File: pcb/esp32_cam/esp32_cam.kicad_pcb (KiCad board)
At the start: 2 copper layers, 31.3 x 43.3 mm, 45 parts, among them CN1 ESP32CAM_P1, CN2 ESP-PSRAM32, CN3 Cam_Connector, CN4 ESP32CAM_P2, CN5 microSD_esp32Cam, Q1 S8050, Q2 PMOS, SW1 SWITCH, U1 ESP32-S(CAM), U2 AMS1117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

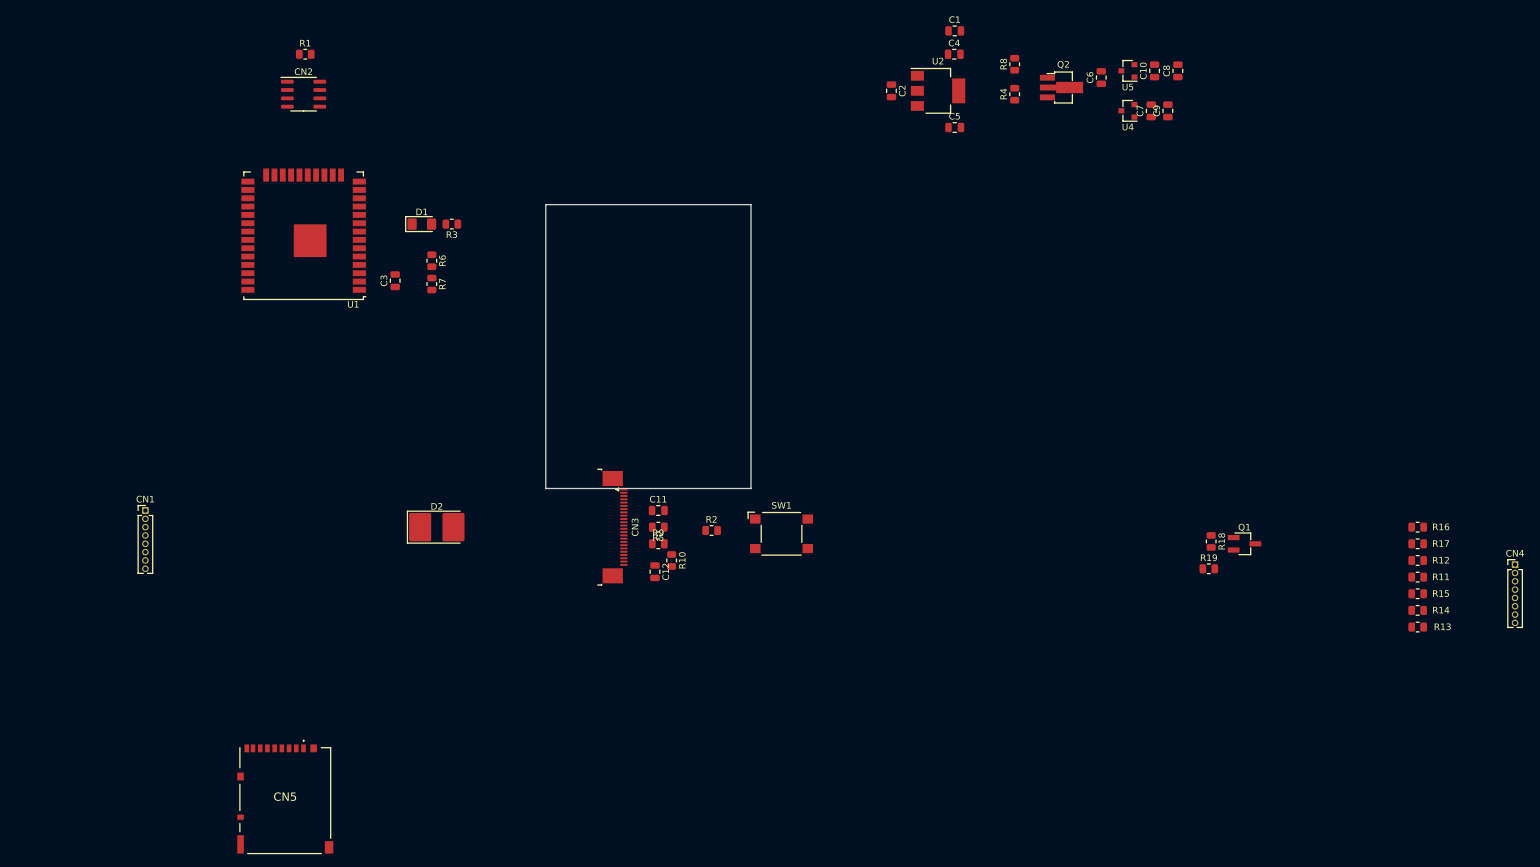
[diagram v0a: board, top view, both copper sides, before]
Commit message: correcciones de esquematico y se agrega y completa  información
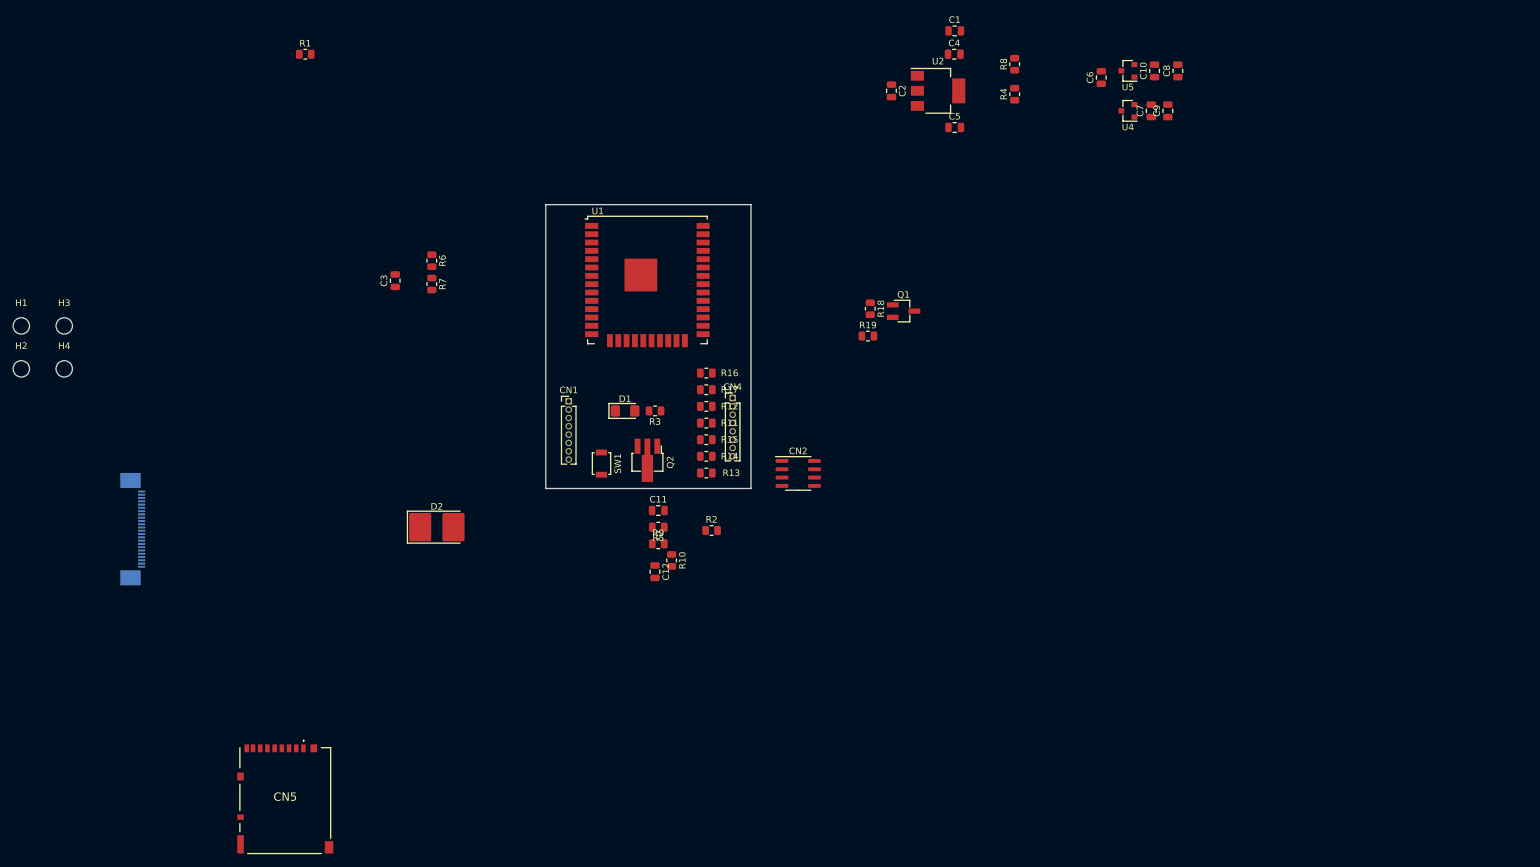
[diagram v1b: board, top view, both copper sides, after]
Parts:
- added H1: MountingHole, MountingHole:MountingHole_2.5mm, F.Cu at (-30.0, 68.5)
- added H2: MountingHole, MountingHole:MountingHole_2.5mm, F.Cu at (-30.0, 75.0)
- added H3: MountingHole, MountingHole:MountingHole_2.5mm, F.Cu at (-23.4, 68.5)
- added H4: MountingHole, MountingHole:MountingHole_2.5mm, F.Cu at (-23.4, 75.0)
- CN3: moved to B.Cu
- SW1: footprint Button_Switch_SMD:SW_SPST_Omron_B3FS-101xP -> Button_Switch_SMD:SW_SPST_B3U-1000P
- moved CN4 122.0 mm to (78.5, 79.5)
- moved R11 111.0 mm to (74.5, 83.3)
- moved R12 111.0 mm to (74.5, 80.8)
- moved R13 111.0 mm to (74.5, 90.9)
- moved R14 111.0 mm to (74.5, 88.4)
- moved R15 111.0 mm to (74.5, 85.9)
- moved R16 111.0 mm to (74.5, 75.7)
- moved R17 111.0 mm to (74.5, 78.2)
- moved CN2 95.1 mm to (88.5, 91.0)
- moved Q2 85.0 mm to (65.5, 89.0), turned to 270 degrees
- moved CN3 73.6 mm to (-13.0, 99.5), turned to 90 degrees
- moved CN1 66.7 mm to (53.5, 80.0)
- moved Q1 63.0 mm to (104.6, 66.2)
- moved R19 63.0 mm to (99.1, 70.0)
- moved R18 63.0 mm to (99.5, 65.9)
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
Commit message: se sube primera versión del PCB
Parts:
- C10, C11, C12, C3, C6, C7, C8, C9, CN5, D2, R10, R11, R12, R13, R14, R15, R16, R17, R18, R19, R9, U4, U5: moved to B.Cu
- CN1, CN4: footprint Connector_PinHeader_1.27mm:PinHeader_1x08_P1.27mm_Vertical -> Connector_PinHeader_2.54mm:PinHeader_1x08_P2.54mm_Vertical
- H3, H4: footprint MountingHole:MountingHole_2.5mm -> MountingHole:MountingHole_2.1mm
- Q1: footprint Package_TO_SOT_SMD:SC-59_Handsoldering -> Package_TO_SOT_SMD:SOT-23; moved to B.Cu
- Q2: footprint Package_TO_SOT_SMD:SOT-89-3_Handsoldering -> Package_TO_SOT_SMD:SOT-23; moved to B.Cu
- moved H2 111.6 mm to (79.2, 52.1)
- moved H4 104.2 mm to (79.5, 91.4)
- moved C8 88.1 mm to (69.8, 73.2), turned to 270 degrees
- moved C10 87.0 mm to (67.6, 73.2), turned to 270 degrees
- moved U5 85.9 mm to (64.8, 73.2)
- moved CN3 85.6 mm to (65.2, 64.8), turned to 0 degrees
- moved C6 84.4 mm to (61.2, 72.1), turned to 270 degrees
- moved H1 83.4 mm to (51.8, 52.1)
- moved R1 82.5 mm to (67.9, 88.9), turned to 90 degrees
- moved C9 82.3 mm to (69.8, 69.6), turned to 270 degrees
- moved C7 82.1 mm to (67.6, 69.6), turned to 270 degrees
- moved U4 81.4 mm to (64.8, 69.6)
- moved CN5 78.9 mm to (65.7, 84.2), turned to 180 degrees
- moved H3 78.7 mm to (51.8, 91.4)
- moved R8 76.5 mm to (54.1, 64.8), turned to 270 degrees
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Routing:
- net GND: track 0.00 -> 193.9 mm, vias 0 -> 11
- net +3V3: track 0.00 -> 172.9 mm, vias 0 -> 6
- net Net-(CN1-Pad4): track 0.00 -> 64.3 mm, vias 0 -> 1
- net /TWI_SCK: track 0.00 -> 61.7 mm, vias 0 -> 2
- net /HS2_DATA1: track 0.00 -> 52.4 mm, vias 0 -> 6
- net Net-(C3-Pad2): track 0.00 -> 49.1 mm, vias 0 -> 3
- net /HS2_DATA0: track 0.00 -> 46.3 mm, vias 0 -> 1
- net Net-(CN3-Pad3): track 0.00 -> 44.1 mm, vias 0 -> 3
- net +5V: track 0.00 -> 39.6 mm
- net /HS2_CMD: track 0.00 -> 34.7 mm, vias 0 -> 2
- net /CSI_MCLK: track 0.00 -> 32.7 mm, vias 0 -> 3
- net Net-(C11-Pad1): track 0.00 -> 27.7 mm, vias 0 -> 1
- net /TWI_SDA: track 0.00 -> 27.4 mm, vias 0 -> 3
- net Net-(C12-Pad1): track 0.00 -> 25.8 mm, vias 0 -> 2
- net Net-(D1-Pad1): track 0.00 -> 25.6 mm, vias 0 -> 2
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- added copper zone on B.Cu, net GND
- added copper zone on F.Cu, net GND
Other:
- board text added: "GRID COLOCAR COMPONENTES: 0,5 mm (20 mils) GRID TRAZAR BORDES: 0,1 mm (3,94 mils) GRID TRAZAR PISTAS: 0,25 mm (9,84 mils)"
- board text added: "Réplica ESP32-CAM DCI - CESE - FIUBA G. CARDOZO"
- board text removed: "GRID COLOCAR COMPONENTES: 0,5 mm (20 MILS) GRID TRAZAR BORDES: 0,1 mm (3,94 mils)"

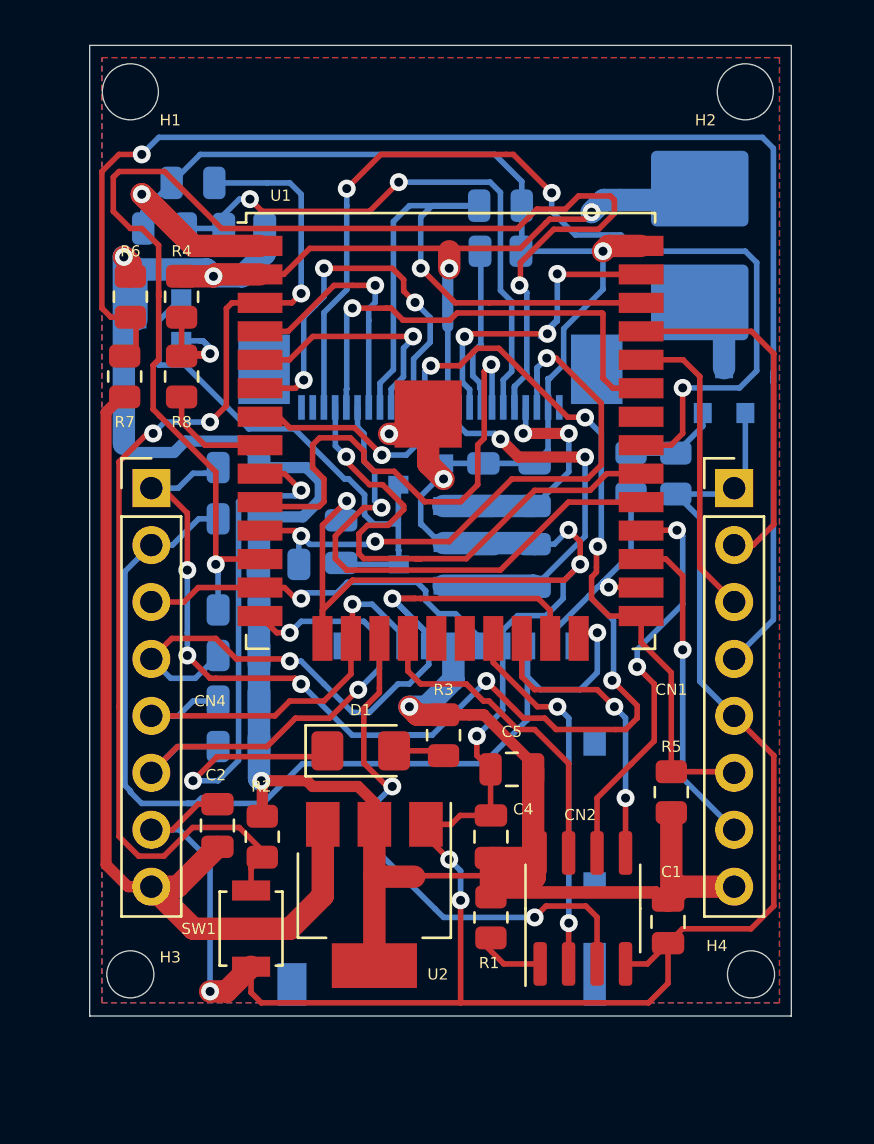
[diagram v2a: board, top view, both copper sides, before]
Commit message: se sube versión final y se agrega documentación
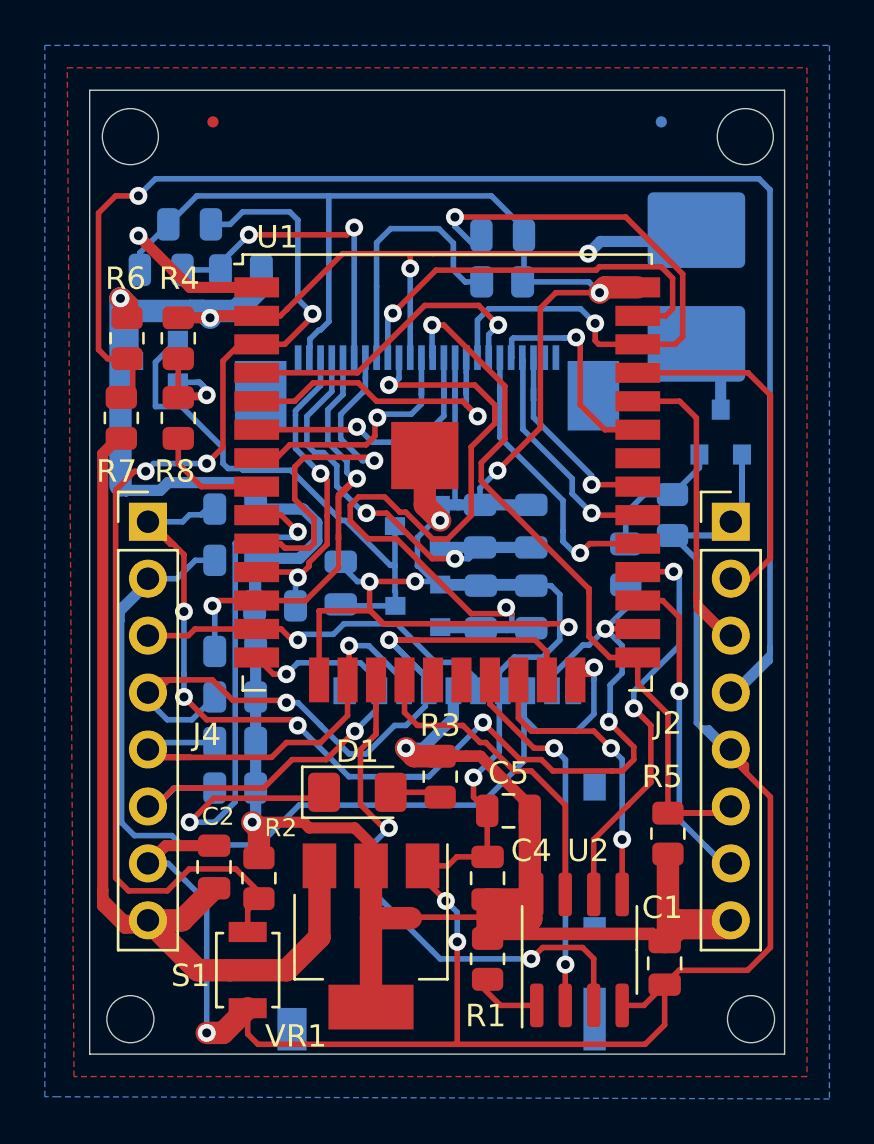
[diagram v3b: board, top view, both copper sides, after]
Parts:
- removed CN1: ESP32CAM_P1, Connector_PinHeader_2.54mm:PinHeader_1x08_P2.54mm_Vertical
- removed CN2: ESP-PSRAM32, Package_SO:SOIC-8_3.9x4.9mm_P1.27mm
- removed CN3: Cam_Connector, Connector_FFC-FPC:TE_2-1734839-4_1x24-1MP_P0.5mm_Horizontal
- removed CN4: ESP32CAM_P2, Connector_PinHeader_2.54mm:PinHeader_1x08_P2.54mm_Vertical
- removed SW1: SWITCH, Button_Switch_SMD:SW_SPST_B3U-1000P
- removed U4: XC6206-2,8V, Package_TO_SOT_SMD:SOT-23
- removed U5: XC6206-1,2V, Package_TO_SOT_SMD:SOT-23
- added H5: Fiducial, Fiducial:Fiducial_0.5mm_Mask1mm, F.Cu at (55.5, 53.4)
- added H6: Fiducial, Fiducial:Fiducial_0.5mm_Mask1mm, B.Cu at (75.5, 53.4)
- added J1: Cam_Connector, Connector_FFC-FPC:TE_2-1734839-4_1x24-1MP_P0.5mm_Horizontal, B.Cu at (65.0, 65.3)
- added J2: ESP32CAM_P1, Connector_PinHeader_2.54mm:PinHeader_1x08_P2.54mm_Vertical, F.Cu at (78.6, 71.2)
- added J4: ESP32CAM_P2, Connector_PinHeader_2.54mm:PinHeader_1x08_P2.54mm_Vertical, F.Cu at (52.6, 71.2)
- added S1: SWITCH, Button_Switch_SMD:SW_SPST_B3U-1000P, F.Cu at (57.0, 91.2)
- added VR1: AMS1117, Package_TO_SOT_SMD:SOT-223-3_TabPin2, F.Cu at (62.5, 89.8)
- added VR2: XC6206-2,8V, Package_TO_SOT_SMD:SOT-23, B.Cu at (64.6, 71.4)
- added VR3: XC6206-1,2V, Package_TO_SOT_SMD:SOT-23, B.Cu at (64.6, 75.0)
- U2: value AMS1117 -> ESP-PSRAM32; footprint Package_TO_SOT_SMD:SOT-223-3_TabPin2 -> Package_SO:SOIC-8_3.9x4.9mm_P1.27mm
- moved U2 9.47 mm to (71.8, 90.3), turned to 90 degrees
- moved R19 4.07 mm to (73.9, 73.2)
- moved H1 2.00 mm to (51.8, 54.1)
- moved H2 2.00 mm to (79.2, 54.1)
- moved H3 2.00 mm to (51.8, 93.4)
- moved H4 2.00 mm to (79.5, 93.4)
- moved J3 2.00 mm to (65.7, 86.2)
- moved C2 1.86 mm to (55.5, 86.7)
- moved C4 1.86 mm to (67.8, 87.2)
- moved R15 1.86 mm to (56.5, 79.1)
- moved R16 1.86 mm to (56.5, 77.0)
- moved R18 1.86 mm to (76.0, 71.0)
- moved R2 1.86 mm to (57.5, 87.2)
- moved R7 1.86 mm to (51.4, 66.6)
- moved R8 1.86 mm to (54.0, 66.6)
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- renumbered CN5 to J3
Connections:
- R1 pad 1: Net-(CN2-Pad1) -> Net-(R1-Pad1)
- U1 pad 17: Net-(CN2-Pad3) -> Net-(U1-Pad17)
- U1 pad 18: Net-(CN2-Pad7) -> Net-(U1-Pad18)
- U1 pad 21: Net-(CN2-Pad2) -> Net-(U1-Pad21)
- U1 pad 22: Net-(CN2-Pad5) -> Net-(U1-Pad22)
- U1 pad 28: Net-(CN2-Pad6) -> Net-(U1-Pad28)
- U2 pad 1: GND -> Net-(R1-Pad1)
- U2 pad 2: +3V3 -> Net-(U1-Pad21)
- U2 pad 3: +5V -> Net-(U1-Pad17)
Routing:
- net /TWI_SCK: track 61.7 -> 21.1 mm
- net Net-(J1-Pad3): track 44.1 -> 9.36 mm, vias 3 -> 1
- net Net-(CN2-Pad3): track 24.3 -> 0.00 mm, vias 2 -> 0
- net Net-(U1-Pad17): track 0.00 -> 24.3 mm, vias 0 -> 2
- net GND: track 193.9 -> 212.2 mm
- net Net-(U1-Pad28): track 0.00 -> 18.3 mm, vias 0 -> 2
- net Net-(CN2-Pad6): track 18.3 -> 0.00 mm, vias 2 -> 0
- net Net-(U1-Pad21): track 0.00 -> 16.4 mm, vias 0 -> 2
- net Net-(CN2-Pad2): track 16.4 -> 0.00 mm, vias 2 -> 0
- net +1V2: track 21.9 -> 37.1 mm
- net Net-(CN2-Pad7): track 14.3 -> 0.00 mm
- net Net-(U1-Pad18): track 0.00 -> 14.3 mm
- net Net-(J1-Pad4): track 24.2 -> 10.3 mm
- net Net-(CN2-Pad5): track 13.1 -> 0.00 mm, vias 2 -> 0
- net Net-(U1-Pad22): track 0.00 -> 13.1 mm, vias 0 -> 2
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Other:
- board size 31.3 x 43.3 mm -> 31 x 43 mm
- board text added: "DATOS DEL FABRICANTE: Circuitos Impresos SEI Gavilán 3660 (1419) Buenos Aires – Argentina Tel/Fax: 4574-5009 / 4573-5807 E-mail: info@seicircuits.com Web site: www.seicircuits.com.ar DESTINATARIO DEL PRODUCTO : GERMÁN E. CARDOZO FECHA 16/08/2021 NOMBRE DEL PRODUCTO/ INSUMO: Circuito Impreso Doble Faz - PCB CÓDIGO DEL INSUMO Código cliente: Réplica ESP32-CAM ESPECIFICACIÓN Según Gerbers CONTROLES 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"
- board text added: "GRID COLOCAR COMPONENTES: 0,5 mm (20 mils) GRID TRAZAR BORDES: 0,5 mm (3,94 mils) GRID TRAZAR PISTAS: 0,25 mm (9,84 mils)"
- board text removed: "GRID COLOCAR COMPONENTES: 0,5 mm (20 mils) GRID TRAZAR BORDES: 0,1 mm (3,94 mils) GRID TRAZAR PISTAS: 0,25 mm (9,84 mils)"

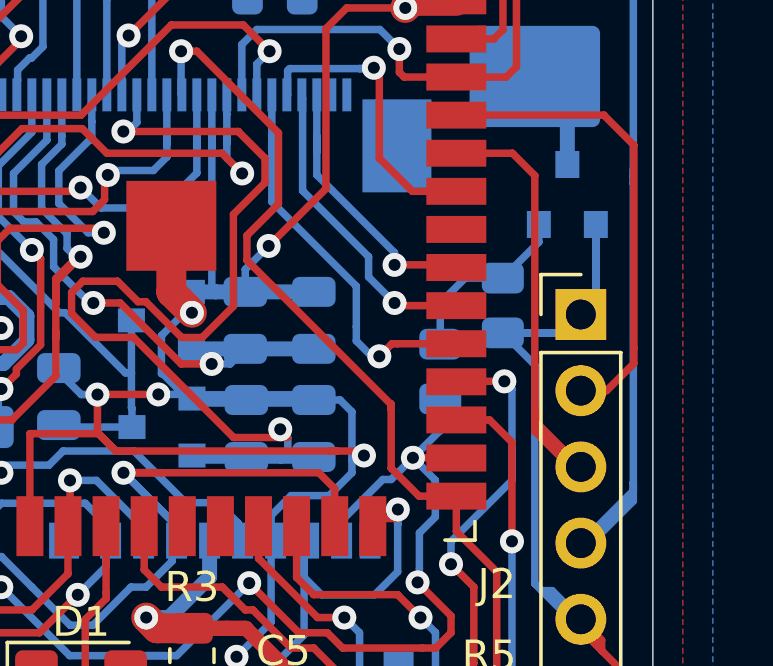
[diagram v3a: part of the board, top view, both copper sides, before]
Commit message: se corrige serigrafía
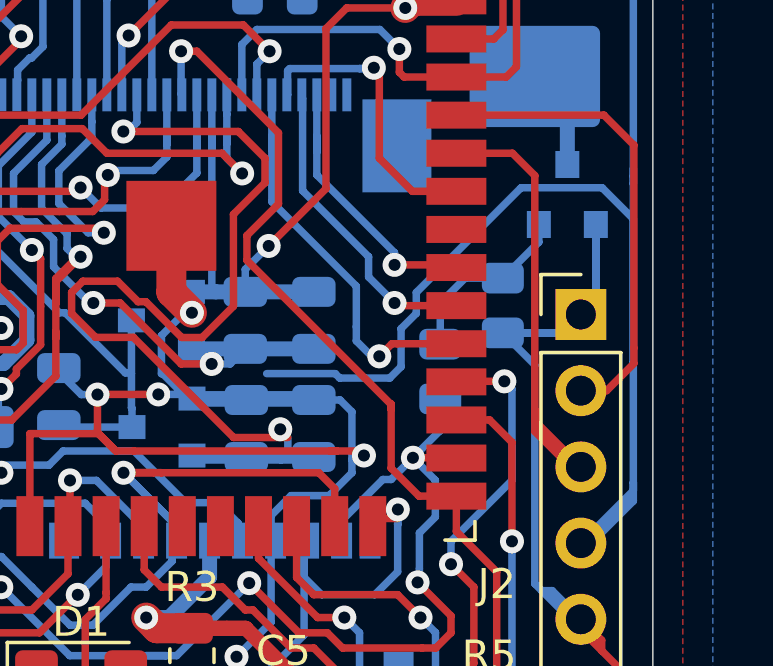
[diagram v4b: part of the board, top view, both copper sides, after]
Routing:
- net Net-(J2-Pad4): track 67.1 -> 88.3 mm
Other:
- board text added: "3V3"
- board text added: "5V"
- board text added: "GND"
- board text added: "GRID COLOCAR COMPONENTES: 0,5 mm (20 mils) GRID TRAZAR BORDES: 0,5 mm (3,94 mils) GRID TRAZAR PISTAS: 0,25 mm (9,84 mils) GRID COLOCAR SERIGRAFÍA 0,25 mm (9,84 mils)"
- board text added: "IO0"
- board text added: "IO12"
- board text added: "IO13"
- board text added: "IO14"
- board text added: "IO15"
- board text added: "IO16"
- board text added: "IO2"
- board text added: "IO4"
- board text added: "UOR"
- board text added: "UOT"
- board text added: "VCC"
- board text removed: "GRID COLOCAR COMPONENTES: 0,5 mm (20 mils) GRID TRAZAR BORDES: 0,5 mm (3,94 mils) GRID TRAZAR PISTAS: 0,25 mm (9,84 mils)"

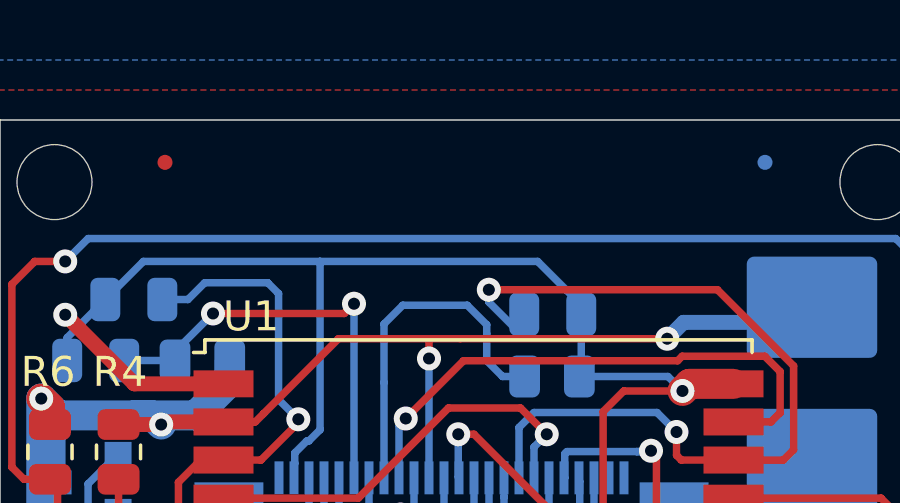
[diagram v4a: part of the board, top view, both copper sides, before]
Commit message: se crea la carpeta shapes3D
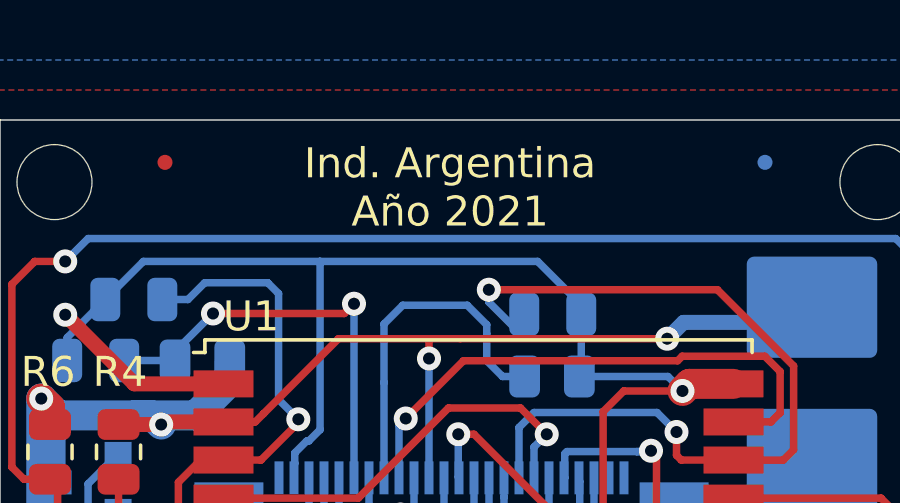
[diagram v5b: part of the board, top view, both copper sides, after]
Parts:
- renumbered H5 to FID1, H6 to FID2
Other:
- board text added: "GRILLAS: COLOCAR COMPONENTES: 0,5 mm (20 mils) TRAZAR BORDES: 0,5 mm (3,94 mils) TRAZAR PISTAS: 0,25 mm (9,84 mils) COLOCAR SERIGRAFÍA 0,25 mm (9,84 mils)"
- board text added: "Ind. Argentina Año 2021"
- board text removed: "GRID COLOCAR COMPONENTES: 0,5 mm (20 mils) GRID TRAZAR BORDES: 0,5 mm (3,94 mils) GRID TRAZAR PISTAS: 0,25 mm (9,84 mils) GRID COLOCAR SERIGRAFÍA 0,25 mm (9,84 mils)"
